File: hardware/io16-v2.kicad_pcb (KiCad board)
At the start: 2 copper layers, 75 x 35 mm, 39 parts, among them J1 AKL_5_2, J10 AKL_5_2, J11 AKL_5_2, J12 AKL_5_2, J13 AKL_5_2, J2 AKL_5_2, J3 AKL_5_2, J4 AKL_5_2, J5 AKL_5_2, J6 AKL_5_2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

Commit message: set origin
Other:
- board text added: "IO-16 2.0"
- board text removed: "IO-16"
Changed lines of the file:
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@@
-(kicad_pcb (version 4) (host pcbnew 4.0.7-e2-6376~58~ubuntu17.04.1)
+(kicad_pcb (version 4) (host pcbnew 4.0.7-e2-6376~61~ubuntu18.04.1)
   (general
     (links 81)
@@
   (layers
     (0 Vorderseite signal)
-    (31 Rückseite signal)
+    (31 Rückseite signal hide)
     (32 B.Adhes user)
     (33 F.Adhes user)
@@
     (pad_drill 1.2)
     (pad_to_mask_clearance 0)
-    (aux_axis_origin 111.5 114.53)
-    (grid_origin 111.5 114.53)
+    (aux_axis_origin 111.5 79.53)
+    (grid_origin 111.5 79.53)
     (visible_elements FFFFFFBF)
     (pcbplotparams
@@
     (effects (font (size 1.00076 1.00076) (thickness 0.14986)))
   )
-  (gr_text IO-16 (at 115.29822 87.92464) (layer F.SilkS)
+  (gr_text "IO-16\n2.0" (at 115.29822 87.92464) (layer F.SilkS)
     (effects (font (size 1.39954 1.39954) (thickness 0.14986)))
   )

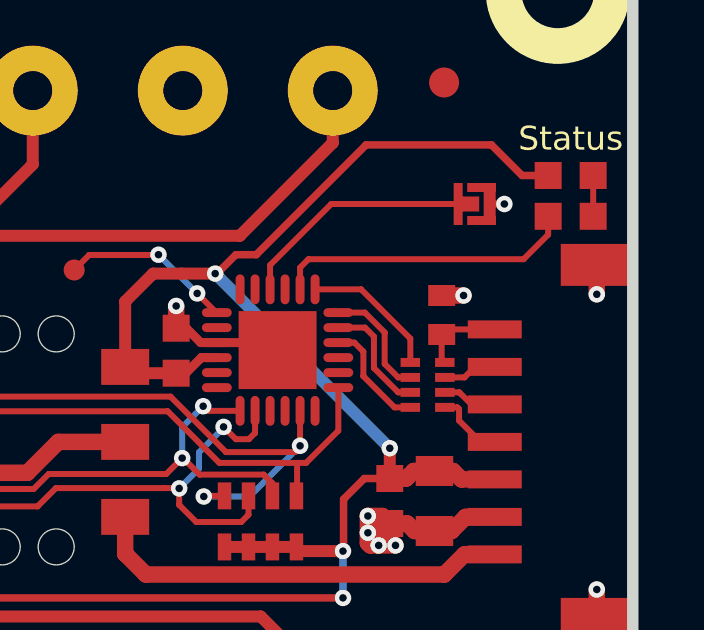
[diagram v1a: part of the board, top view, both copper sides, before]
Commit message: Change capacitor footprint(s) to C0402F
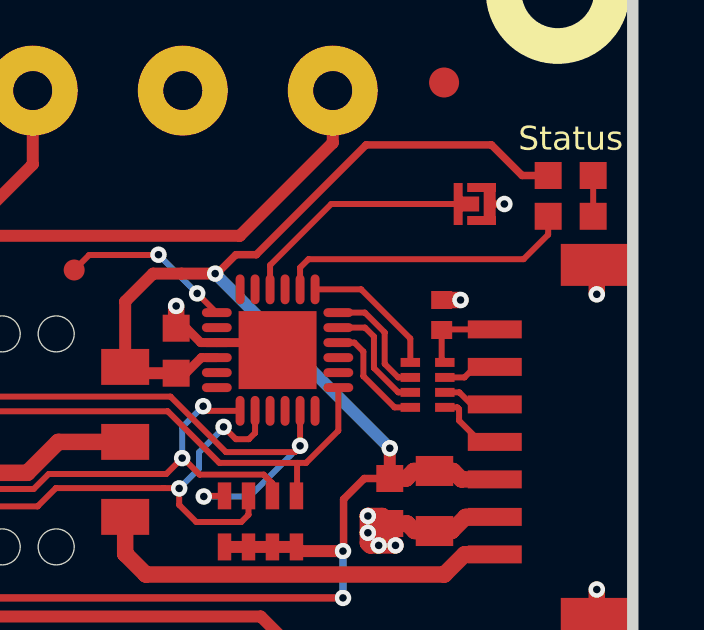
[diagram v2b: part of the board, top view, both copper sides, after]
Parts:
- C1: footprint C0805 -> kicad-libraries:C0805
- C2, C3, C5, C6: footprint C0603F -> kicad-libraries:C0603F
- C4: footprint C0402E -> kicad-libraries:C0402F
- D1: footprint D0603F -> kicad-libraries:D0603F
- R1: footprint R0603F -> kicad-libraries:R0603F
- RP1: footprint 4X0603 -> kicad-libraries:4X0603
- RP2: footprint 4X0402 -> kicad-libraries:4X0402

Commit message: fix text
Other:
- board text removed: "2.0"
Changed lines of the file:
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@@
-(kicad_pcb (version 4) (host pcbnew 4.0.2+dfsg1-stable)
+(kicad_pcb (version 4) (host pcbnew 4.0.7-e2-6376~61~ubuntu18.04.1)
   (general
     (links 81)
     (no_connects 0)
-    (area 111.309499 79.339499 186.690501 114.720501)
+    (area 15.62915 78.674999 187.355001 194.490793)
     (thickness 1.6002)
-    (drawings 47)
+    (drawings 46)
     (tracks 340)
     (zones 0)
@@
   )
   (setup
-    (last_trace_width 0.55)
+    (last_trace_width 0.24892)
     (user_trace_width 0.2)
     (user_trace_width 0.25)
@@
     (effects (font (size 0.8001 0.8001) (thickness 0.200025)))
   )
-  (gr_text 2.0 (at 115.65128 107.24896) (layer F.SilkS)
-    (effects (font (size 1.00076 1.00076) (thickness 0.14986)))
-  )
   (gr_text - (at 112.52454 99.55022 90) (layer F.SilkS)
     (effects (font (size 1.50114 1.50114) (thickness 0.37592)))
@@
   (gr_line (start 161.509668 98.533628) (end 161.509668 97.631929) (angle 90) (layer F.SilkS) (width 0.17018))
   (gr_text 5V (at 161.5 100.63 90) (layer F.SilkS)
-    (effects (font (size 1.19888 1.19888) (thickness 0.14986)))
+    (effects (font (size 1 1) (thickness 0.14986)))
   )
   (gr_text 3.3V (at 161.5 94.43 90) (layer F.SilkS)
-    (effects (font (size 1.19888 1.19888) (thickness 0.14986)))
+    (effects (font (size 1 1) (thickness 0.14986)))
   )
   (gr_text B7 (at 176.49952 113.4237) (layer F.SilkS)
@@
   )
   (gr_text "IO-16\n2.0" (at 115.29822 87.92464) (layer F.SilkS)
-    (effects (font (size 1.39954 1.39954) (thickness 0.14986)))
+    (effects (font (size 1 1) (thickness 0.14986)))
   )
   (segment (start 180.13 92.3) (end 180.76 92.3) (width 0.55) (layer Vorderseite) (net 1))

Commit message: specify processor
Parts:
- U1: value XMC1XXX24 -> XMC11XX24
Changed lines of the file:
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@@
       (effects (font (size 0.3 0.3) (thickness 0.075)))
     )
-    (fp_text value XMC1XXX24 (at 0 0.8 270) (layer F.Fab)
+    (fp_text value XMC11XX24 (at 0 0.8 270) (layer F.Fab)
       (effects (font (size 0.3 0.3) (thickness 0.075)))
     )

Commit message: specify multiplexer ic
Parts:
- U8: value PCAL6416A -> PCAL6416APW
